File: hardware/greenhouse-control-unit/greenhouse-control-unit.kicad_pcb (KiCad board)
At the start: 4 copper layers, 150 x 99.9 mm, 83 parts, among them J1 Molex_KK-396_01x02, J10 Conn_ESP32_DevKitV1_Female, J11 Conn_01x05_Female, J12 Conn_01x05_Female, J14 Molex_KK-254_01x12, J15 Molex_KK-396_01x02, J2 Molex_KK-396_01x02, J3 Beep_Jumper, J4 PV Buck, J5 Conn_01x08_Male, J6 5V Buck, J8 Conn_01x09, J9 Conn_01x05_Female, Q1 2N7000, Q10 2N7000, Q11 FDP7030BL, Q12 FDP7030BL, Q13 2N7002, Q14 STD30NF06LT4, Q15 2N7002, Q16 STD30NF06LT4, Q17 2N7002, Q18 2N7002, Q19 STD30NF06LT4, Q2 BC547, Q20 STD30NF06LT4, Q3 TN0702, Q4 2N7000, Q5 FDP7030BL, Q6 BC547, Q7 BC337, Q8 FDP7030BL, Q9 FDP7030BL, U1 PCF8574, U2 PCF8574, U3 ZXCT1107, U4 ZXCT1107

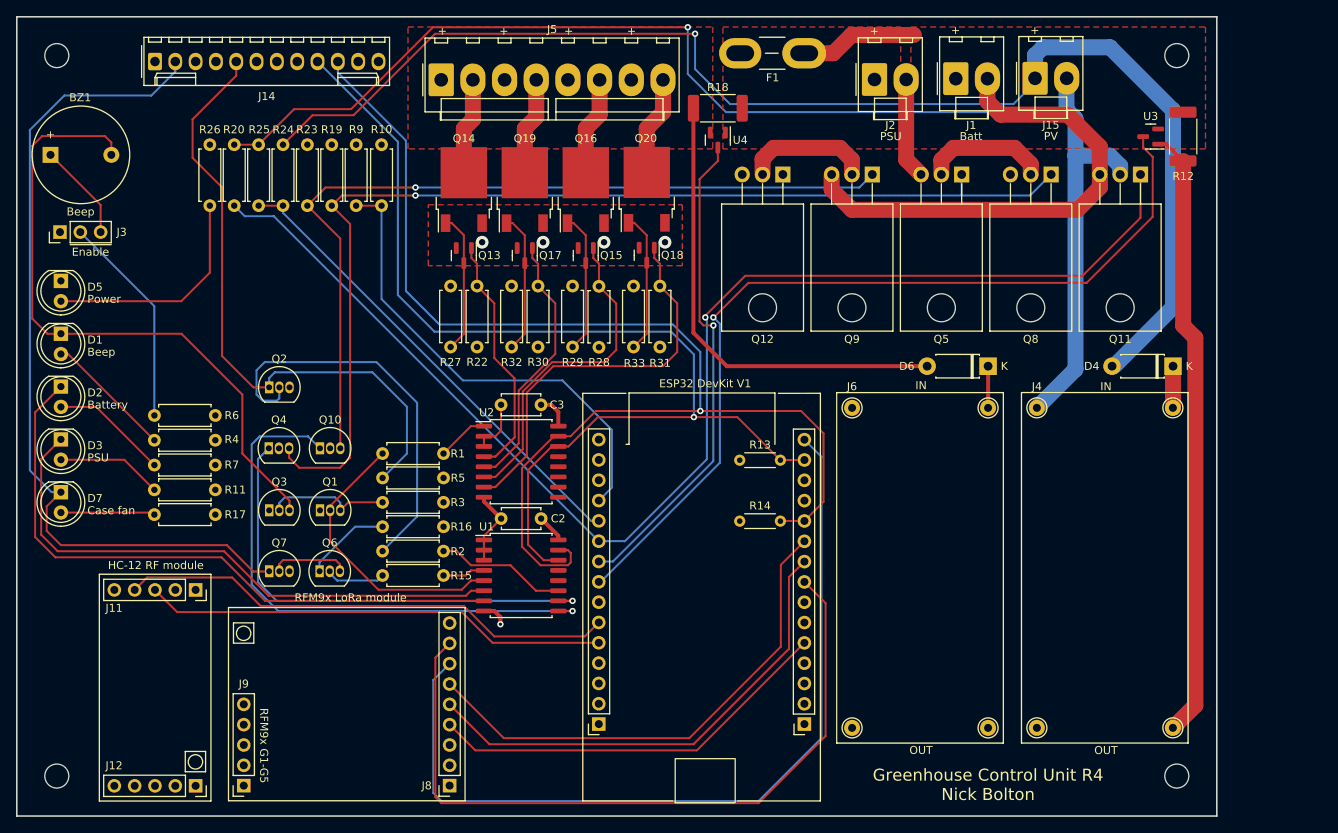
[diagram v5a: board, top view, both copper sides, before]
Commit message: Separate battery and PV voltage sensors
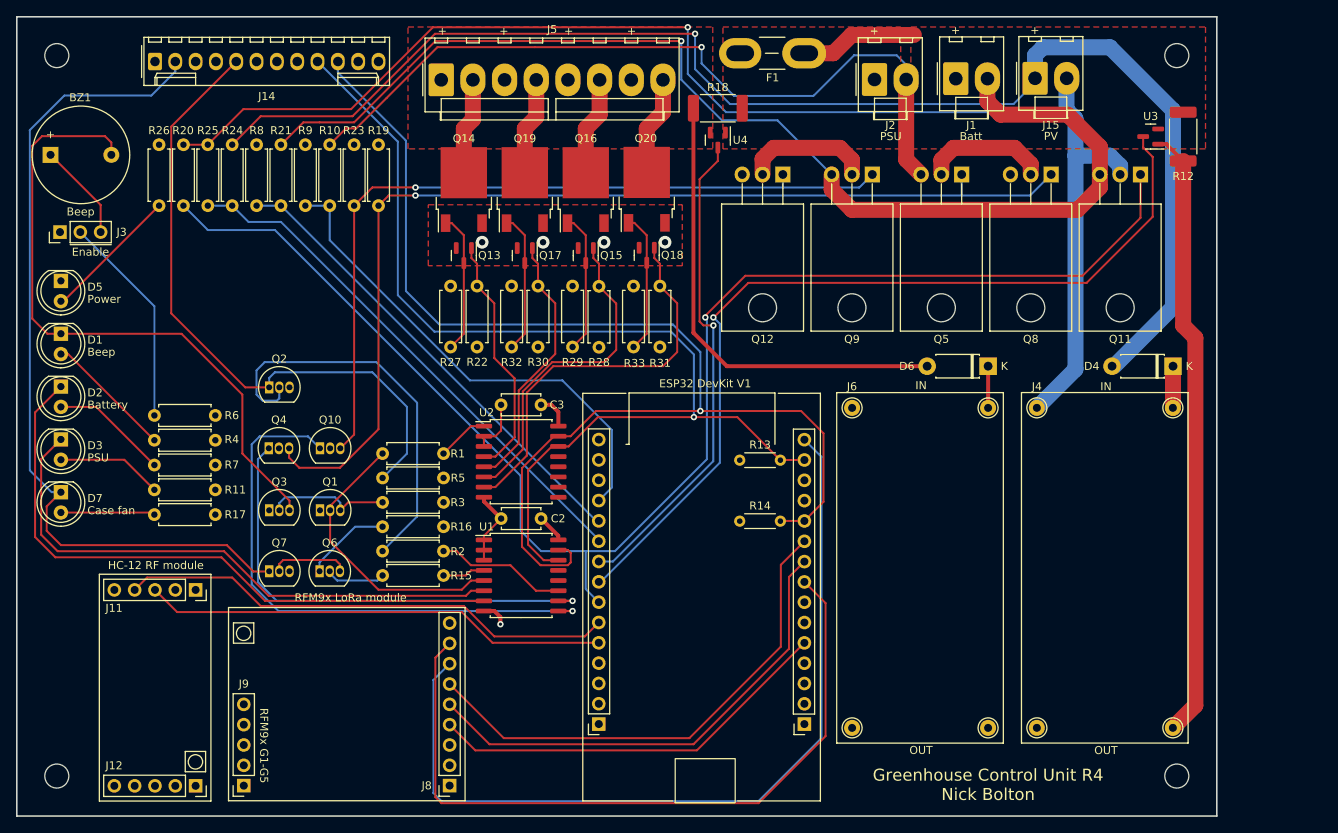
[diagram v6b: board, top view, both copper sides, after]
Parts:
- added R21: 100k, Resistor_THT:R_Axial_DIN0207_L6.3mm_D2.5mm_P7.62mm_Horizontal, F.Cu at (105.2, 58.2)
- added R8: 1M, Resistor_THT:R_Axial_DIN0207_L6.3mm_D2.5mm_P7.62mm_Horizontal, F.Cu at (102.1, 50.5)
- moved R10 6.48 mm to (111.3, 58.2)
- moved R26 6.35 mm to (89.9, 50.5)
- moved R9 6.35 mm to (108.2, 50.5)
- moved R20 6.35 mm to (93.0, 50.5)
- moved R24 6.35 mm to (99.1, 50.5)
- moved R25 6.35 mm to (96.0, 58.2)
- moved R19 5.84 mm to (117.3, 58.2)
- moved R23 5.84 mm to (114.3, 58.2)
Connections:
- net /Common_VS renamed /PSU_VS
- J10 pad 10: /PV_PWM -> /PV_VS
- J10 pad 11: /PV_VS -> /Batt_VS
- J10 pad 7: unconnected-(J10-Pad7) -> /PV_PWM
- R10 pad 2: GND -> /PSU_GND
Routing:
- net /PSU_GND: track 12.6 -> 97.9 mm, vias 0 -> 1
- net /Batt_GND: track 61.9 -> 145.9 mm, vias 0 -> 1
- net /Batt_VS: track 0.00 -> 59.1 mm
- net /PV_PWM: track 163.6 -> 182.0 mm
- net Net-(D5-Pad2): track 28.5 -> 17.2 mm
- net /PV_VS: track 59.4 -> 66.4 mm
- net Net-(Q10-Pad3): track 105.9 -> 99.1 mm
- net /PV_Vcc: track 165.9 -> 172.3 mm
- net /PV_GND: track 171.5 -> 177.9 mm
- net Net-(Q4-Pad3): track 136.4 -> 131.1 mm
- net +3V3: track 67.9 -> 72.9 mm
- net /PsuRelayNC_IN: track 78.7 -> 81.5 mm
- net /PSU_VS: track 59.9 -> 62.0 mm

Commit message: Tweak traces
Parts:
- moved BZ1 7.98 mm to (84.3, 51.8), turned to 180 degrees
- moved J3 0.46 mm to (78.0, 61.5)
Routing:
- net Net-(BZ1-Pad2): track 80.9 -> 68.7 mm
- net Net-(BZ1-Pad1): track 12.2 -> 10.2 mm
- net +3V3: track 72.9 -> 71.3 mm
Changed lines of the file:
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@@
   (net 102 "unconnected-(J8-Pad3)")
   (footprint "Connector_PinHeader_2.54mm:PinHeader_1x03_P2.54mm_Vertical" (layer "F.Cu")
-    (at 77.5358 61.468 90)
+    (at 77.993 61.468 90)
     (descr "Through hole straight pin header, 1x03, 2.54mm pitch, single row")
     (tags "Through hole pin header THT 1x03 2.54mm single row")
@@
   )
   (footprint "Buzzer_Beeper:Buzzer_12x9.5RM7.6" (layer "F.Cu")
-    (at 76.3524 51.816)
+    (at 84.328 51.816 180)
     (descr "Generic Buzzer, D12mm height 9.5mm with RM7.6mm")
     (tags "buzzer")
@@
     (property "Sheetname" "")
     (attr through_hole)
-    (fp_text reference "BZ1" (at 3.7084 -7.1628) (layer "F.SilkS")
+    (fp_text reference "BZ1" (at 3.8 7.112) (layer "F.SilkS")
       (effects (font (size 1 1) (thickness 0.15)))
     )
-    (fp_text value "10mA beep" (at 3.7592 -5.4356 180) (layer "F.Fab")
+    (fp_text value "10mA beep" (at 3.7592 2.54) (layer "F.Fab")
       (effects (font (size 1 1) (thickness 0.15)))
     )
@@
       (effects (font (size 1 1) (thickness 0.15)))
     )
-    (fp_text user "${REFERENCE}" (at 3.8 0 180) (layer "F.Fab")
+    (fp_text user "${REFERENCE}" (at 3.8 0) (layer "F.Fab")
       (effects (font (size 1 1) (thickness 0.15)))
     )
@@
     (fp_circle (center 3.8 0) (end 4.8 0) (layer "F.Fab") (width 0.1) (fill none))
     (fp_circle (center 3.8 0) (end 9.8 0) (layer "F.Fab") (width 0.1) (fill none))
-    (pad "1" thru_hole rect (at 0 0) (size 2 2) (drill 1) (layers *.Cu *.Mask)
+    (pad "1" thru_hole rect (at 0 0 180) (size 2 2) (drill 1) (layers *.Cu *.Mask)
       (net 2 "Net-(BZ1-Pad1)") (pinfunction "-") (pintype "passive"))
-    (pad "2" thru_hole circle (at 7.6 0) (size 2 2) (drill 1) (layers *.Cu *.Mask)
+    (pad "2" thru_hole circle (at 7.6 0 180) (size 2 2) (drill 1) (layers *.Cu *.Mask)
       (net 19 "Net-(BZ1-Pad2)") (pinfunction "+") (pintype "passive"))
     (model "${KICAD6_3DMODEL_DIR}/Buzzer_Beeper.3dshapes/Buzzer_12x9.5RM7.6.wrl"
@@
   (gr_rect (start 82.4553 104.2416) (end 96.3999 132.588) (layer "F.SilkS") (width 0.15) (fill none))
   (gr_rect (start 95.7348 128.9284) (end 93.1948 126.3884) (layer "F.SilkS") (width 0.15) (fill none))
-  (gr_line (start 83.9366 63.0428) (end 78.8058 63.0428) (layer "F.SilkS") (width 0.15))
+  (gr_line (start 84.3938 63.0428) (end 79.263 63.0428) (layer "F.SilkS") (width 0.15))
   (gr_rect (start 101.759 112.856425) (end 99.219 110.316425) (layer "F.SilkS") (width 0.15) (fill none))
   (gr_rect (start 128.1696 108.3978) (end 98.5994 132.5532) (layer "F.SilkS") (width 0.15) (fill none))
@@
   (via (at 130.302 62.738) (size 1.6) (drill 0.8) (layers "F.Cu" "B.Cu") (free) (net 1))
   (via (at 153.162 62.738) (size 1.6) (drill 0.8) (layers "F.Cu" "B.Cu") (free) (net 1))
-  (segment (start 82.6158 61.468) (end 82.6158 58.0794) (width 0.25) (layer "F.Cu") (net 2))
-  (segment (start 82.6158 58.0794) (end 76.3524 51.816) (width 0.25) (layer "F.Cu") (net 2))
+  (segment (start 83.073 61.468) (end 84.4024 60.1386) (width 0.25) (layer "F.Cu") (net 2))
+  (segment (start 84.4024 60.1386) (end 84.4024 51.816) (width 0.25) (layer "F.Cu") (net 2))
   (segment (start 121.3975 102.3765) (end 121.3975 112.1265) (width 0.5) (layer "In1.Cu") (net 3))
   (segment (start 193.548 130.81) (end 193.548 123.444) (width 0.5) (layer "In1.Cu") (net 3))
+  (segment (start 86.614 67.7672) (end 86.614 42.946) (width 0.5) (layer "In1.Cu") (net 3))
+  (segment (start 86.614 42.946) (end 89.408 40.152) (width 0.5) (layer "In1.Cu") (net 3))
+  (segment (start 81.026 73.3552) (end 86.614 67.7672) (width 0.5) (layer "In1.Cu") (net 3))
   (segment (start 144.841003 133.731) (end 144.884 133.688003) (width 0.5) (layer "In1.Cu") (net 3))
   (segment (start 96.9518 96.784) (end 92.8978 100.838) (width 0.5) (layer "In1.Cu") (net 3))
-  (segment (start 81.026 73.3552) (end 86.0044 68.3768) (width 0.5) (layer "In1.Cu") (net 3))
   (segment (start 92.8978 100.838) (end 81.026 100.838) (width 0.5) (layer "In1.Cu") (net 3))
   (segment (start 190.669997 133.688003) (end 193.548 130.81) (width 0.5) (layer "In1.Cu") (net 3))
   (segment (start 144.884 133.688003) (end 144.884 122.9675) (width 0.5) (layer "In1.Cu") (net 3))
-  (segment (start 86.0044 43.5556) (end 89.408 40.152) (width 0.5) (layer "In1.Cu") (net 3))
-  (segment (start 86.0044 68.3768) (end 86.0044 43.5556) (width 0.5) (layer "In1.Cu") (net 3))
   (segment (start 121.3975 112.1265) (end 121.3975 130.5415) (width 0.5) (layer "In1.Cu") (net 3))
-  (segment (start 81.026 100.838) (end 81.026 73.3552) (width 0.5) (layer "In1.Cu") (net 3))
   (segment (start 121.3975 130.5415) (end 124.587 133.731) (width 0.5) (layer "In1.Cu") (net 3))
   (segment (start 144.884 133.688003) (end 190.669997 133.688003) (width 0.5) (layer "In1.Cu") (net 3))
+  (segment (start 81.026 100.838) (end 81.026 73.3552) (width 0.5) (layer "In1.Cu") (net 3))
   (segment (start 121.3975 112.1265) (end 84.4405 112.1265) (width 0.5) (layer "In1.Cu") (net 3))
   (segment (start 125.476 98.298) (end 121.3975 102.3765) (width 0.5) (layer "In1.Cu") (net 3))
@@
   (segment (start 138.938 83.058) (end 137.668 83.058) (width 0.5) (layer "F.Cu") (net 4))
   (segment (start 139.8276 85.725) (end 139.8276 83.9476) (width 0.5) (layer "F.Cu") (net 4))
+  (segment (start 114.808 40.152) (end 114.808 41.656) (width 0.5) (layer "In1.Cu") (net 4))
   (segment (start 114.808 41.656) (end 112.141 44.323) (width 0.5) (layer "In1.Cu") (net 4))
+  (segment (start 89.8398 44.323) (end 87.63 46.5328) (width 0.5) (layer "In1.Cu") (net 4))
+  (segment (start 87.63 46.5328) (end 87.63 72.8218) (width 0.5) (layer "In1.Cu") (net 4))
   (segment (start 112.141 44.323) (end 89.8398 44.323) (width 0.5) (layer "In1.Cu") (net 4))
-  (segment (start 87.4776 46.6852) (end 87.4776 69.215) (width 0.5) (layer "In1.Cu") (net 4))
-  (segment (start 87.4776 69.215) (end 91.0844 72.8218) (width 0.5) (layer "In1.Cu") (net 4))
-  (segment (start 114.808 40.152) (end 114.808 41.656) (width 0.5) (layer "In1.Cu") (net 4))
-  (segment (start 89.8398 44.323) (end 87.4776 46.6852) (width 0.5) (layer "In1.Cu") (net 4))
   (segment (start 77.6478 93.985) (end 75.8698 95.763) (width 0.25) (layer "F.Cu") (net 9))
   (segment (start 75.8698 95.763) (end 75.8698 98.816) (width 0.25) (layer "F.Cu") (net 9))
@@
   (segment (start 128.905 103.759) (end 130.5276 103.759) (width 0.25) (layer "F.Cu") (net 18))
   (segment (start 128.27 104.394) (end 128.905 103.759) (width 0.25) (layer "F.Cu") (net 18))
-  (segment (start 75.2856 49.4792) (end 83.1596 49.4792) (width 0.25) (layer "F.Cu") (net 19))
-  (segment (start 74.0664 50.6984) (end 75.2856 49.4792) (width 0.25) (layer "F.Cu") (net 19))
-  (segment (start 75.956 74.178) (end 74.0664 72.2884) (width 0.25) (layer "F.Cu") (net 19))
-  (segment (start 83.9524 50.272) (end 83.9524 51.816) (width 0.25) (layer "F.Cu") (net 19))
+  (segment (start 77.6478 74.178) (end 75.956 74.178) (width 0.25) (layer "F.Cu") (net 19))
   (segment (start 92.72 74.178) (end 77.6478 74.178) (width 0.25) (layer "F.Cu") (net 19))
   (segment (start 106.2228 95.0468) (end 100.33 89.154) (width 0.25) (layer "F.Cu") (net 19))
+  (segment (start 74.0664 72.2884) (end 74.0664 54.4776) (width 0.25) (layer "F.Cu") (net 19))
+  (segment (start 75.956 74.178) (end 74.0664 72.2884) (width 0.25) (layer "F.Cu") (net 19))
   (segment (start 100.33 89.154) (end 100.33 81.788) (width 0.25) (layer "F.Cu") (net 19))
-  (segment (start 77.6478 74.178) (end 75.956 74.178) (width 0.25) (layer "F.Cu") (net 19))
-  (segment (start 83.1596 49.4792) (end 83.9524 50.272) (width 0.25) (layer "F.Cu") (net 19))
-  (segment (start 74.0664 72.2884) (end 74.0664 50.6984) (width 0.25) (layer "F.Cu") (net 19))
+  (segment (start 74.0664 54.4776) (end 76.728 51.816) (width 0.25) (layer "F.Cu") (net 19))
   (segment (start 100.33 81.788) (end 92.72 74.178) (width 0.25) (layer "F.Cu") (net 19))
   (segment (start 106.2228 96.245) (end 106.2228 95.0468) (width 0.25) (layer "F.Cu") (net 19))
@@
   (segment (start 122.174 82.804) (end 122.174 97.028) (width 0.25) (layer "B.Cu") (net 50))
   (segment (start 117.094 77.724) (end 122.174 82.804) (width 0.25) (layer "B.Cu") (net 50))
-  (segment (start 89.3318 70.724) (end 80.0758 61.468) (width 0.25) (layer "B.Cu") (net 52))
-  (segment (start 89.3318 84.3888) (end 89.3318 70.724) (width 0.25) (layer "B.Cu") (net 52))
+  (segment (start 89.3318 84.3888) (end 89.3318 70.2668) (width 0.25) (layer "B.Cu") (net 52))
+  (segment (start 89.3318 70.2668) (end 80.533 61.468) (width 0.25) (layer "B.Cu") (net 52))
   (segment (start 144.5575 97.5675) (end 144.884 97.5675) (width 0.25) (layer "B.Cu") (net 55))
   (segment (start 105.156 58.166) (end 102.108 58.166) (width 0.25) (layer "B.Cu") (net 55))

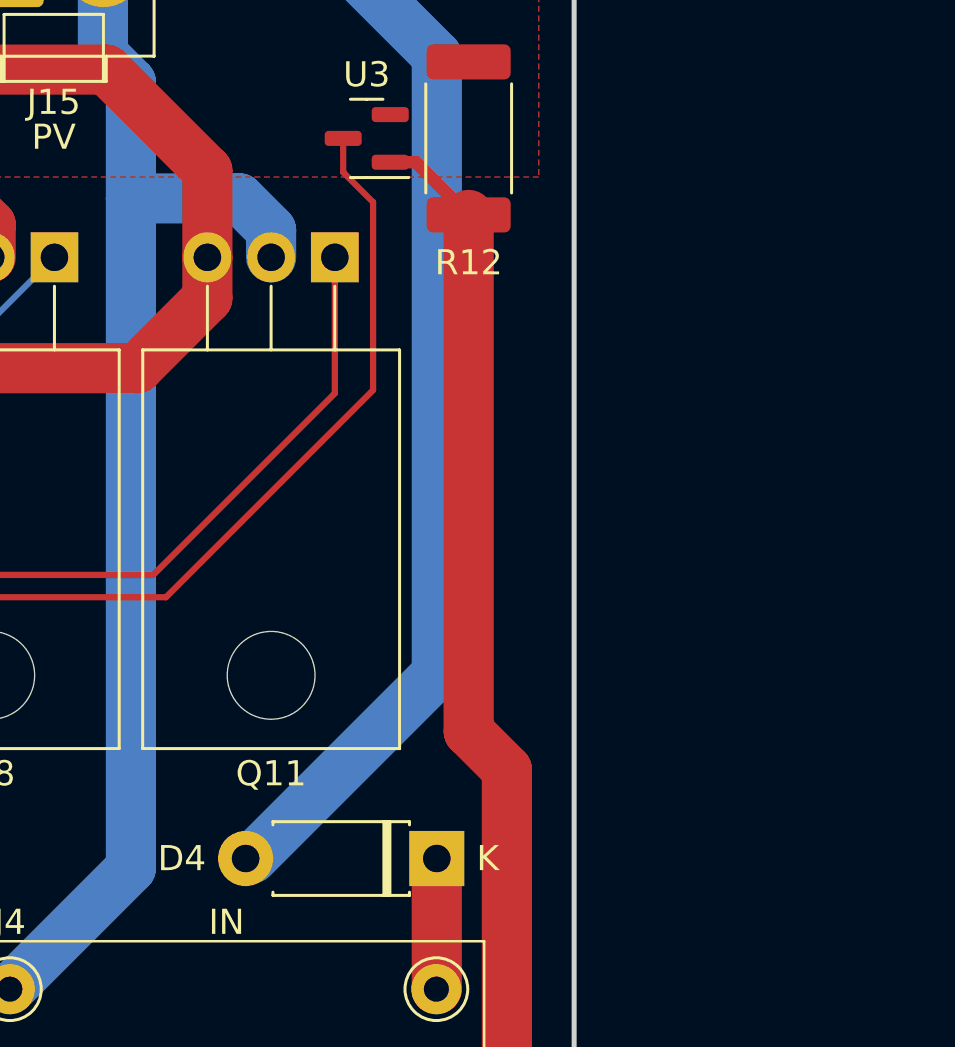
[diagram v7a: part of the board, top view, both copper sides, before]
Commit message: Replace diode with back-to-back FET
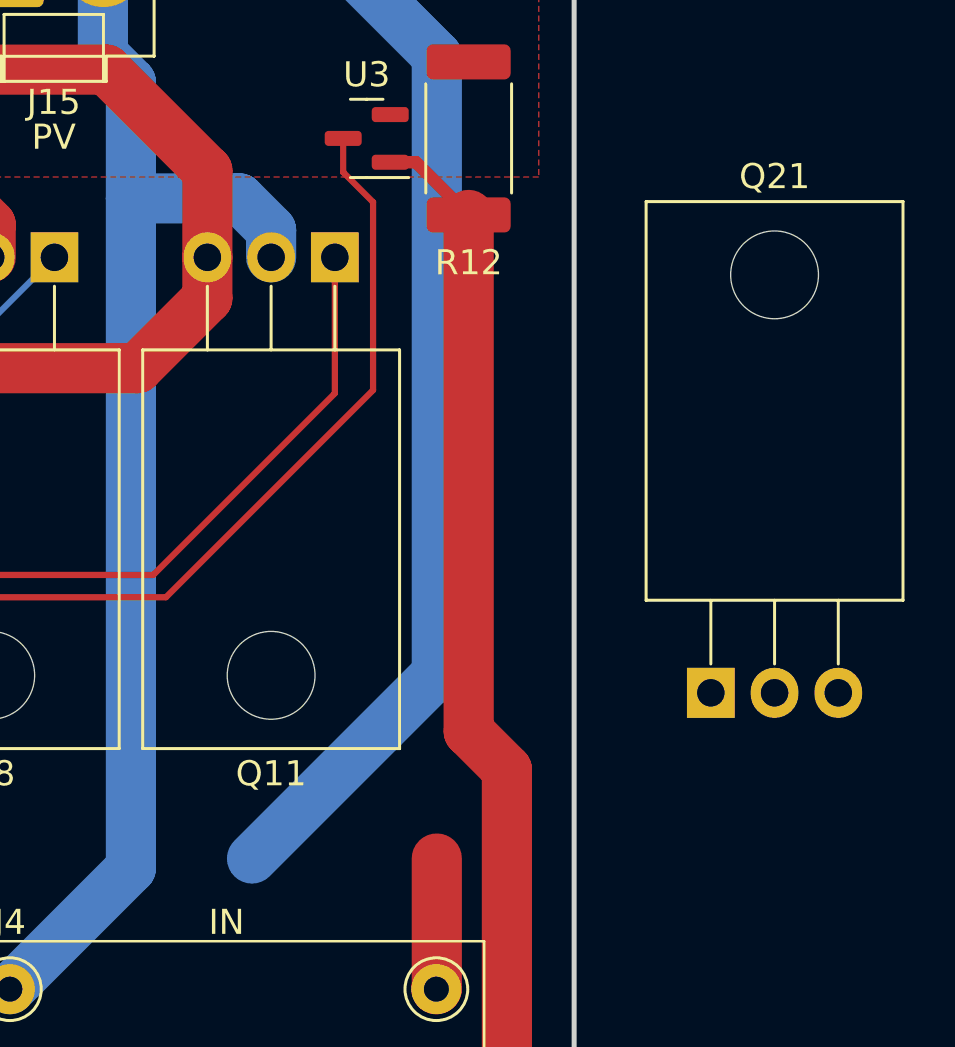
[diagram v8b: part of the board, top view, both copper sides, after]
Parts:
- removed D4: D, Diode_THT:D_DO-41_SOD81_P7.62mm_Horizontal
- added Q21: FDP7030BL, Package_TO_SOT_THT:TO-220-3_Horizontal_TabDown, F.Cu at (227.6, 71.6)
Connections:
- J4 pad 1: Net-(D4-Pad1) -> /PV_Vcc
- Q11 pad 2: /PV_GND -> Net-(Q11-Pad2)
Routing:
- net /PV_Vcc: track 172.3 -> 177.5 mm
- net Net-(D4-Pad1): track 5.21 -> 0.00 mm
